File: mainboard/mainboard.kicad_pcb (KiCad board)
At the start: 2 copper layers, 91 x 100 mm, 126 parts, among them J1 Eurorack_Power, J10 H2, J11 CV3, J12 O3, J13 H3, J2 R1, J3 CV1, J4 R2, J5 O1, J6 H1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

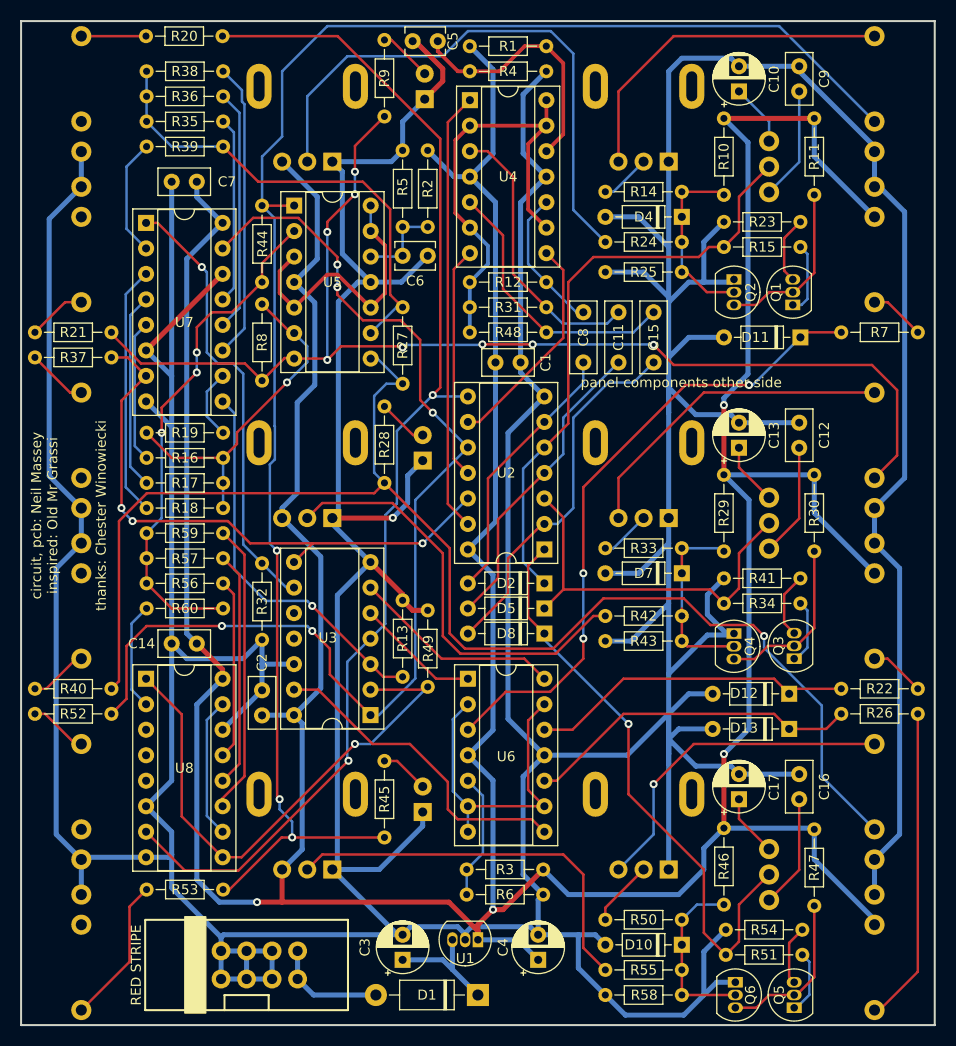
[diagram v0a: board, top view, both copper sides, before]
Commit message: Rerouted: number of vias reduced from 39 to 13
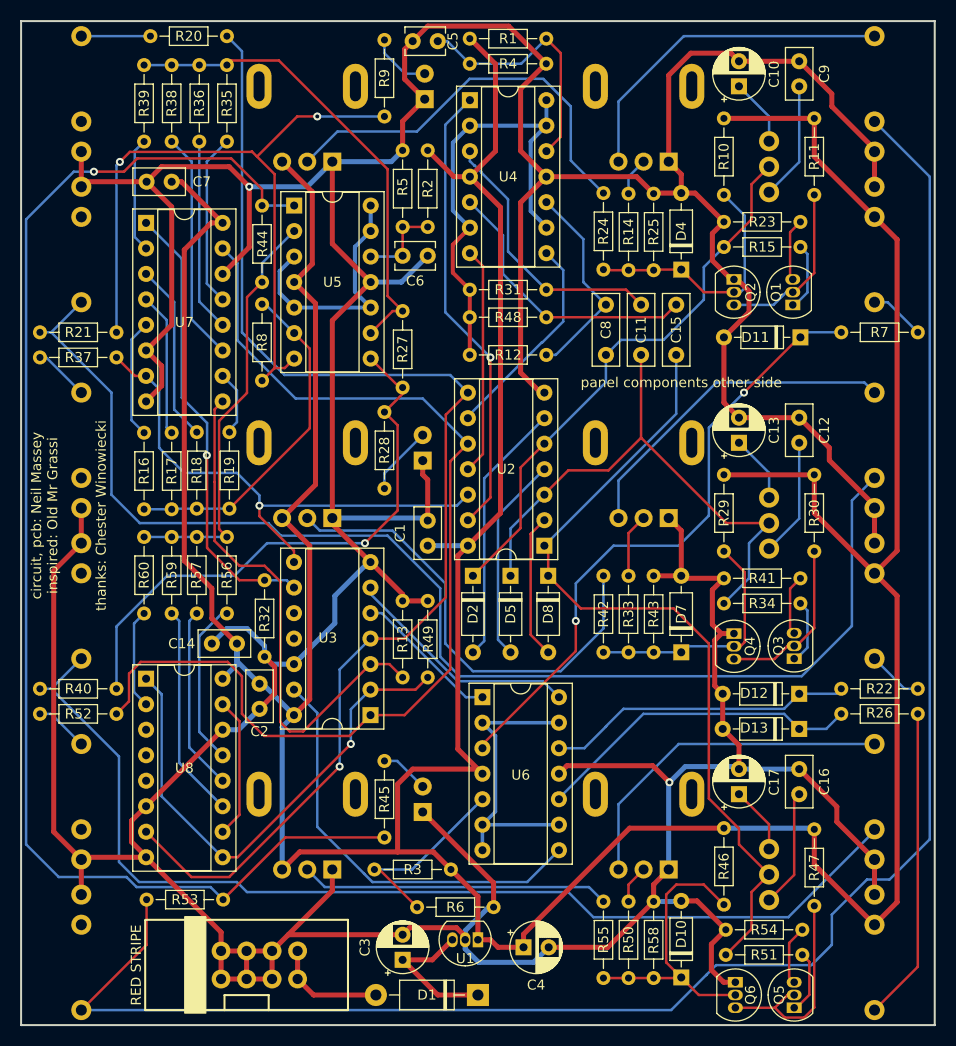
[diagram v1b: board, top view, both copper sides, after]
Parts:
- moved C1 19.5 mm to (54.5, 65.2), turned to 90 degrees
- moved R59 9.50 mm to (29.0, 72.0), turned to 90 degrees
- moved R3 9.19 mm to (56.8, 97.5)
- moved R18 9.06 mm to (31.5, 53.9), turned to -90 degrees
- moved R38 8.67 mm to (29.0, 25.0), turned to 90 degrees
- moved D7 7.87 mm to (79.8, 75.9), turned to 90 degrees
- moved R12 7.25 mm to (58.7, 46.2)
- moved D2 7.16 mm to (59.0, 68.2), turned to -90 degrees
- moved R28 7.06 mm to (50.2, 51.9), turned to -90 degrees
- moved R55 6.81 mm to (72.0, 100.7), turned to -90 degrees
- moved R57 6.09 mm to (31.5, 72.0), turned to 90 degrees
- moved D8 5.76 mm to (66.5, 68.2), turned to -90 degrees
- moved R17 5.59 mm to (29.0, 54.0), turned to -90 degrees
- moved D4 5.25 mm to (79.8, 37.8), turned to 90 degrees
- moved R6 5.10 mm to (53.4, 101.2)
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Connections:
- D2 pad 1: Net-(D2-Pad1) -> Net-(C8-Pad1)
- D2 pad 2: Net-(C8-Pad1) -> Net-(D2-Pad2)
- D5 pad 1: Net-(D5-Pad1) -> Net-(C11-Pad1)
- D5 pad 2: Net-(C11-Pad1) -> Net-(D5-Pad2)
- D8 pad 1: Net-(D8-Pad1) -> Net-(C15-Pad1)
- D8 pad 2: Net-(C15-Pad1) -> Net-(D8-Pad2)
- J10 pad T: Net-(J10-PadT) -> Hav2
- J13 pad T: Net-(J13-PadT) -> Hav3
- J6 pad T: Net-(J6-PadT) -> Hav1
- R15 pad 2: Net-(D2-Pad1) -> Net-(C8-Pad1)
- R21 pad 1: Hav1 -> Net-(R21-Pad1)
- R21 pad 2: Net-(J6-PadT) -> Hav1
- R27 pad 2: Hav2 -> Net-(R27-Pad2)
- R28 pad 1: Hav2 -> Net-(R27-Pad2)
- R34 pad 2: Net-(D5-Pad1) -> Net-(C11-Pad1)
- R40 pad 1: Hav2 -> Net-(R27-Pad2)
- R40 pad 2: Net-(J10-PadT) -> Hav2
- R44 pad 2: Hav3 -> Net-(R44-Pad2)
- R45 pad 1: Hav3 -> Net-(R44-Pad2)
- R51 pad 2: Net-(D8-Pad1) -> Net-(C15-Pad1)
- R53 pad 1: Hav3 -> Net-(R44-Pad2)
- R53 pad 2: Net-(J13-PadT) -> Hav3
- R8 pad 2: Hav1 -> Net-(R21-Pad1)
- R9 pad 1: Hav1 -> Net-(R21-Pad1)
- SW1 pad 2: Net-(D2-Pad1) -> Net-(C8-Pad1)
- SW2 pad 2: Net-(D5-Pad1) -> Net-(C11-Pad1)
- SW3 pad 2: Net-(D8-Pad1) -> Net-(C15-Pad1)
- U2 pad 1: Net-(D8-Pad1) -> Net-(C15-Pad1)
- U2 pad 2: Net-(C15-Pad1) -> Net-(D8-Pad2)
- U2 pad 3: Net-(D5-Pad1) -> Net-(C11-Pad1)
- U2 pad 4: Net-(C11-Pad1) -> Net-(D5-Pad2)
- U2 pad 5: Net-(D2-Pad1) -> Net-(C8-Pad1)
- U2 pad 6: Net-(C8-Pad1) -> Net-(D2-Pad2)
- U5 pad 1: Hav3 -> Net-(R44-Pad2)
- U5 pad 7: Hav1 -> Net-(R21-Pad1)
- U5 pad 8: Hav2 -> Net-(R27-Pad2)
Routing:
- net GND: track 856.3 -> 626.1 mm, vias 1 -> 2
- net Net-(R44-Pad2): track 0.00 -> 134.9 mm, vias 0 -> 1
- net Net-(R21-Pad1): track 0.00 -> 71.6 mm, vias 0 -> 2
- net Net-(D2-Pad1): track 59.6 -> 0.00 mm
- net Net-(D8-Pad1): track 59.0 -> 0.00 mm, vias 1 -> 0
- net Net-(R27-Pad2): track 0.00 -> 56.9 mm, vias 0 -> 1
- net Net-(C15-Pad1): track 37.0 -> 81.7 mm
- net Net-(D5-Pad1): track 38.9 -> 0.00 mm
- net Hav2: track 138.7 -> 106.7 mm, vias 1 -> 0
- net Net-(C8-Pad1): track 26.8 -> 55.5 mm
- net Net-(D2-Pad2): track 0.00 -> 26.3 mm
- net Net-(C11-Pad1): track 30.7 -> 55.9 mm
- net +9V: track 468.0 -> 443.3 mm, vias 4 -> 0
- net Net-(D5-Pad2): track 0.00 -> 20.7 mm
- net Net-(R24-Pad1): track 56.7 -> 40.8 mm
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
